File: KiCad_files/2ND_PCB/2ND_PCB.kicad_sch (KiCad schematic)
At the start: 0 parts

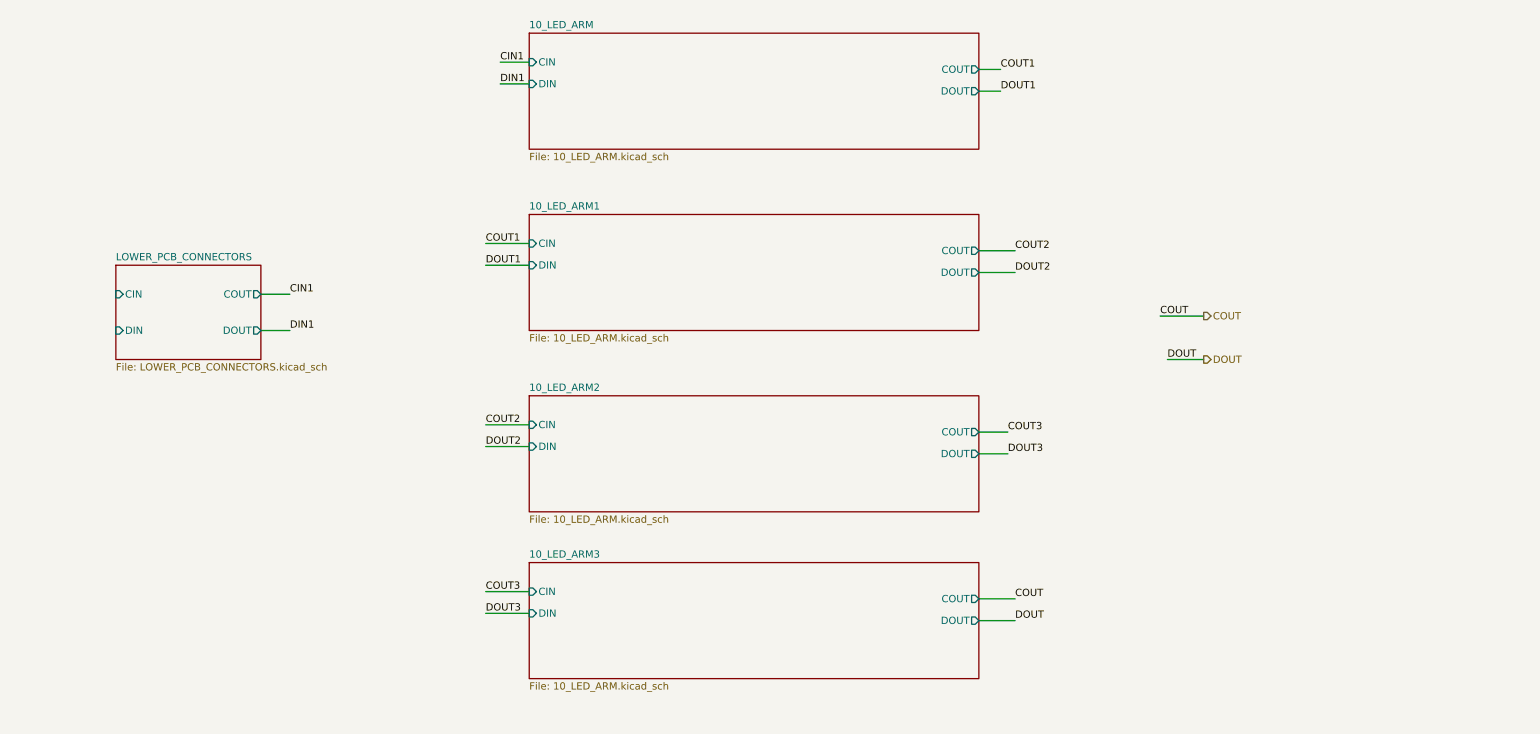
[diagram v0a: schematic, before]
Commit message: Add files via upload
28/8 22:47 -
fixed most errors, still 4 left
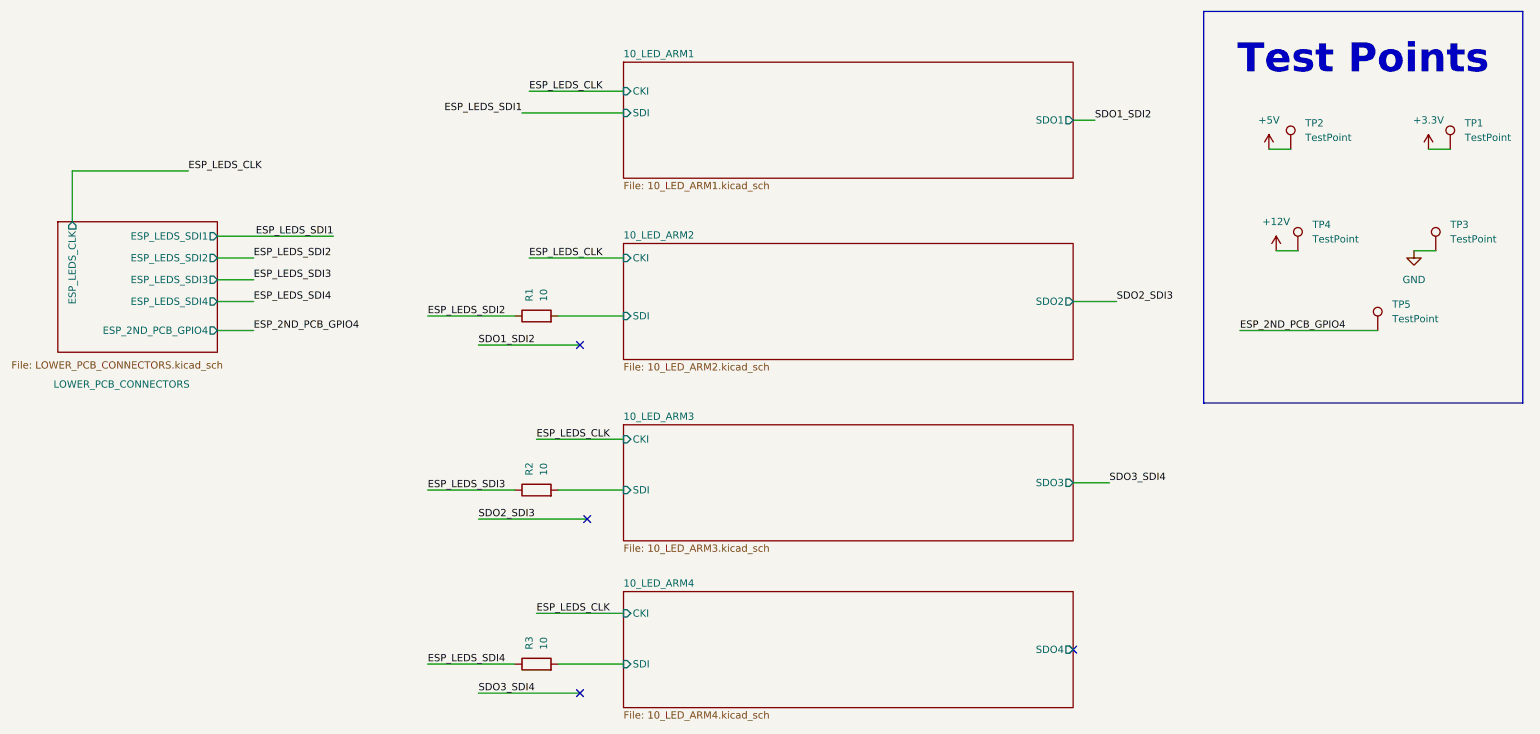
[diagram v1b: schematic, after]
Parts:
- added R1, R2, R3: 10, symbol Device:R
- added TP1, TP2, TP3, TP4, TP5: TestPoint, symbol Connector:TestPoint
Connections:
- new net +12V: TP4.1
- new net +3.3V: TP1.1
- new net +5V: TP2.1
- new net 10_LED_ARM2/SDI: R1.2
- new net 10_LED_ARM3/SDI: R2.2
- new net 10_LED_ARM4/SDI: R3.2
- new net ESP_2ND_PCB_GPIO4: TP5.1
- new net ESP_LEDS_SDI2: R1.1
- new net ESP_LEDS_SDI3: R2.1
- new net ESP_LEDS_SDI4: R3.1
- new net GND: TP3.1
- no-connect marks 0 -> 4
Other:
- removed sheet 10_LED_ARM
- added sheet 10_LED_ARM4 (10_LED_ARM4.kicad_sch)
- sheet 10_LED_ARM1: file 10_LED_ARM.kicad_sch -> 10_LED_ARM1.kicad_sch
- sheet 10_LED_ARM1 ports: added CKI, SDI, SDO1; removed CIN, COUT, DIN, DOUT
- sheet 10_LED_ARM2: file 10_LED_ARM.kicad_sch -> 10_LED_ARM2.kicad_sch
- sheet 10_LED_ARM2 ports: added CKI, SDI, SDO2; removed CIN, COUT, DIN, DOUT
- sheet 10_LED_ARM3: file 10_LED_ARM.kicad_sch -> 10_LED_ARM3.kicad_sch
- sheet 10_LED_ARM3 ports: added CKI, SDI, SDO3; removed CIN, COUT, DIN, DOUT
- sheet LOWER_PCB_CONNECTORS ports: added ESP_2ND_PCB_GPIO4, ESP_LEDS_CLK, ESP_LEDS_SDI1, ESP_LEDS_SDI2, ESP_LEDS_SDI3, ESP_LEDS_SDI4; removed CIN, COUT, DIN, DOUT
- note added: "Test Points"
